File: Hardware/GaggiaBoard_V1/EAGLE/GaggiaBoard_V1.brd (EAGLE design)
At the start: 87 x 122 mm, 113 parts, among them IC1 LD117ADT33TR, J10 PIN262409-1, J11 PIN262409-1, J12 PIN262409-1, J13 PIN262409-1, J14 PIN262409-1, J15 PIN262409-1, J16 PIN262409-1, J17 PIN262409-1, J18 PIN262409-1, J19 PIN262409-1, J2 QWIIC_RIGHT_ANGLE, J20 PIN262409-1, J21 PIN262409-1, J22 PIN262409-1, J23 PIN262409-1, J24 5033981892, J3 QWIIC_RIGHT_ANGLE, J4 1X2-3.5MM, J5 1X2-3.5MM, K1 RELAY-SPDT-JZC-11F, K2 RELAY-SPDT-JZC-11F, K3 RELAY-SPDT-JZC-11F, Q1 600mA/40V, Q2 600mA/40V, Q3 600mA/40V, Q4 600mA/40V, Q5 600mA/40V, Q6 600mA/40V, Q8 600mA/40V, Q9 600mA/40V, U1 BLACKPILL, U2 MAX31855K, U3 MAX31855K, U5 TXS0102, U6 TXU0102

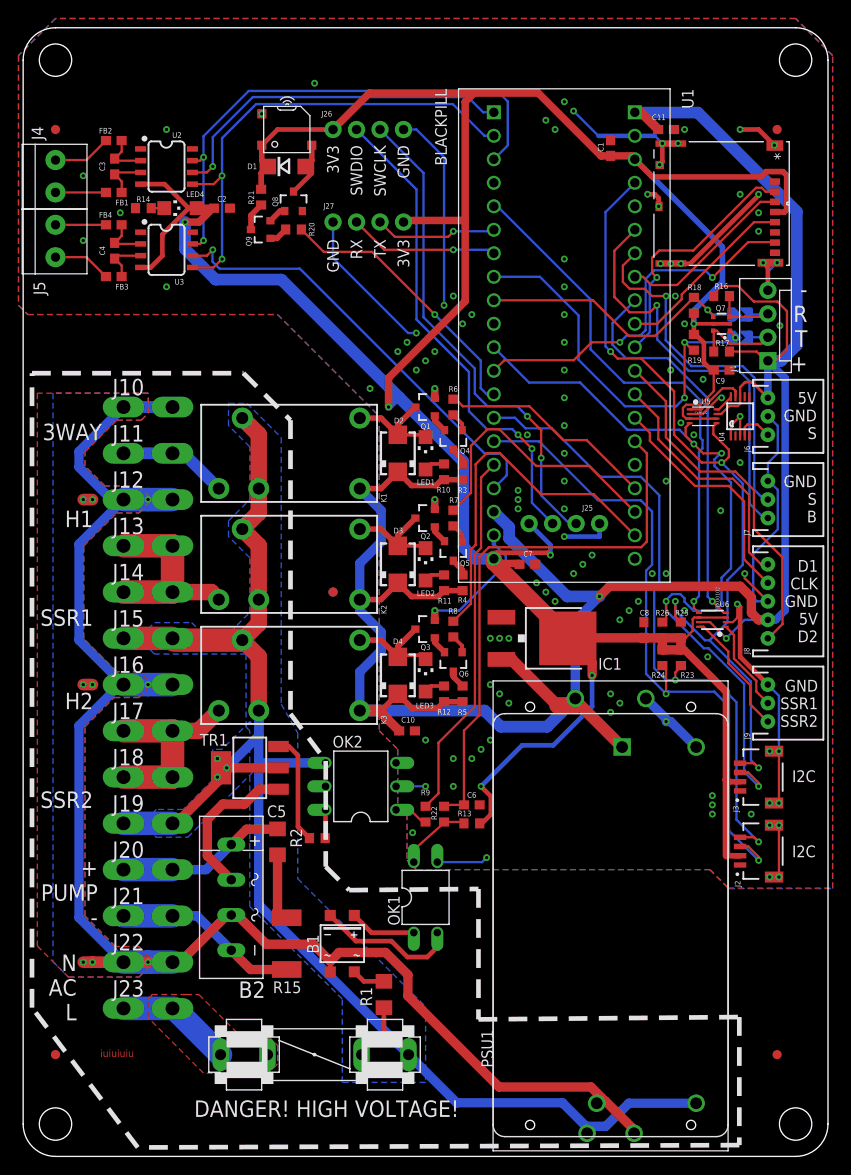
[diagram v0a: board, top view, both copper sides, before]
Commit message: Connectors spacing fixed
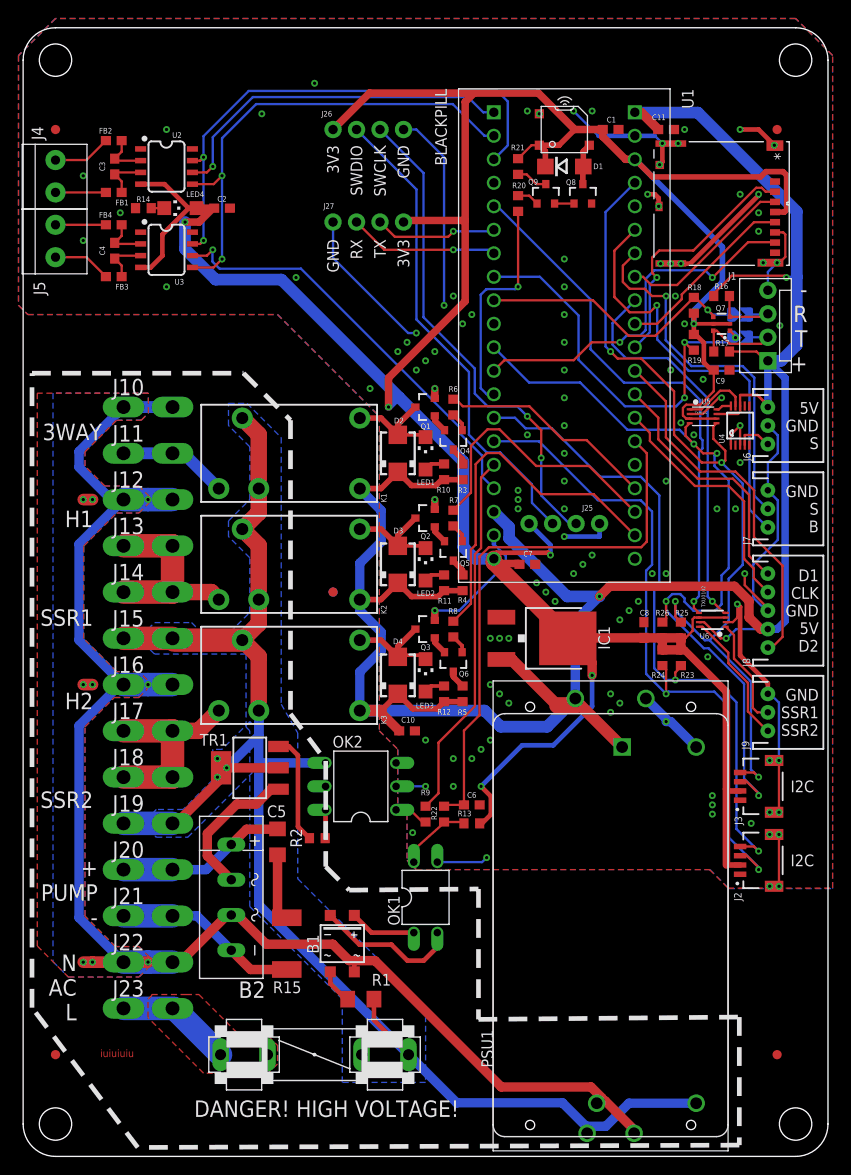
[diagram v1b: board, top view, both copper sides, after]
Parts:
- moved Q8 31.3 mm to (57.0, 93.0)
- moved Q9 31.0 mm to (53.0, 93.0), turned to 0 degrees
- moved D1 30.0 mm to (55.0, 96.0)
- moved SPK1 30.0 mm to (55.0, 100.0)
- moved R21 28.0 mm to (50.0, 96.0)
- moved R20 24.4 mm to (50.0, 92.0), turned to 90 degrees
- moved R1 2.55 mm to (33.0, 6.00), turned to 180 degrees
- moved C1 2.00 mm to (60.0, 100.0), turned to 0 degrees
- moved J2 1.00 mm to (74.0, 21.0)
- moved J3 1.00 mm to (74.0, 29.0)
- moved J6 1.00 mm to (77.0, 68.0)
- moved J7 1.00 mm to (77.0, 59.0)
- moved J8 1.00 mm to (77.0, 48.0)
- moved J9 1.00 mm to (77.0, 37.0)
- moved U4 1.00 mm to (74.0, 68.0)
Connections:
- net AC_N: now also B1.~2; no longer B1.~1
- net N$37: now also B1.~1; no longer B1.~2
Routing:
- net PB5: track 29.9 -> 24.3 mm
- net 5V: track 280.2 -> 275.5 mm, vias 2 -> 3
- net GND: track 183.1 -> 186.1 mm, vias 115 -> 116
- net 3V3: track 349.5 -> 347.3 mm
- net N$30: track 6.75 -> 4.49 mm
- net SPI2_NSS2: track 48.1 -> 46.0 mm
- net AC_N: track 169.8 -> 167.7 mm
- net N$42: track 10.1 -> 11.8 mm
- net AC_P: track 172.6 -> 174.0 mm
- net PA3: track 38.5 -> 39.7 mm
- net I2C1_SCL: track 70.8 -> 71.8 mm
- net PA1: track 26.0 -> 26.9 mm
- net N$41: track 13.7 -> 14.6 mm
- net I2C1_SDA: track 72.7 -> 73.6 mm
- net N$40: track 16.6 -> 15.7 mm
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
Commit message: Layout update
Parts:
- added C12: 1nF/250V, rcl:C0603
- added C13: 10uF/16V, rcl:C0603
- added D5: 1N4007, diode:DO214AC
- added IC2: LD117AS33TR, v-reg:SOT223
- added Q10: 600mA/40V, SparkFun-DiscreteSemi:SOT23-3
- added R27, R28: 10K, rcl:R0603
- IC1: value LD117ADT33TR -> LD117AS33TR; device v-reg:DPACK -> v-reg:SOT223
- J2, J3: value QWIIC_RIGHT_ANGLE -> Vertical Qwiic Connector; device SparkFun-Connectors:JST04_1MM_RA -> SparkFun-Connectors:JST04_1MM_VERT
- J6, J7, J9: device SparkFun-Connectors:JST-3-PTH -> SparkFun-Connectors:JST-3-PTH-VERT
- J8: device SparkFun-Connectors:JST-5-PTH -> SparkFun-Connectors:JST-5-PTH-VERT
- R1: value 220K -> 470; device rcl:R1206 -> rcl:R0603
- R12: value 120 -> 51
- R13: value 10K -> 220; device rcl:R0603 -> rcl:R2512
- R14: value 51 -> 10K
- R15: value 220 -> 1K; device rcl:R2512 -> rcl:R0603
- R20, R21: value 10K -> 220K; device rcl:R0603 -> rcl:R1206
- R22: value 100 -> 22K
- R9: value 470 -> 120
- moved R21 91.2 mm to (30.0, 7.00), turned to 0 degrees
- moved R20 85.8 mm to (38.0, 7.00), turned to 180 degrees
- moved R14 73.6 mm to (43.0, 26.0), turned to 90 degrees
- moved R12 53.3 mm to (20.0, 87.5), turned to 90 degrees
- moved R9 37.1 mm to (42.0, 63.0)
- moved R13 23.9 mm to (25.0, 12.0), turned to 90 degrees
- moved R1 21.2 mm to (40.0, 26.0), turned to 270 degrees
- moved C6 17.6 mm to (39.0, 10.5)
- moved R22 16.6 mm to (30.0, 14.5), turned to 270 degrees
- moved R15 14.0 mm to (39.0, 12.5), turned to 0 degrees
- moved R10 12.0 mm to (42.0, 51.0)
- moved R11 12.0 mm to (42.0, 39.0)
- moved J1 7.65 mm to (78.5, 82.5), turned to 270 degrees
- moved LED4 6.52 mm to (20.0, 92.0), turned to 180 degrees
- moved C2 5.39 mm to (20.0, 96.5), turned to 90 degrees
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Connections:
- new net N$43: C6.2, D5.A, Q10.2
- new net N$44: OK1.1, R15.2
- new net N$45: B1.+, C6.1, R15.1, R22.2
- net 3V3: now also C13.1, IC2.4, R14.2, R27.2; no longer R13.2, R21.2
- net 5V: now also IC2.3, R9.2; no longer R12.2
- net AC_N: now also R21.1; no longer B1.~2
- net AC_P: now also R20.1; no longer R1.1
- net GND: now also C13.2, IC2.1, R12.1; no longer C6.2, R14.1
- net N$2: now also B1.-, D5.C, Q10.1, R22.1; no longer B1.+, OK1.1
- net N$24: now also R9.1; no longer R10.1
- net N$27: now also R12.2; no longer R14.2
- net N$28: now also R10.1; no longer R11.1
- net N$29: now also R11.1; no longer R12.1
- net N$32: now also R13.2; no longer R15.2
- net N$34: now also R28.2; no longer R20.2
- net N$35: now also R27.1; no longer R21.1
- net N$36: now also B1.~1, C12.2, R21.2; no longer OK1.4, R13.1, R22.1
- net N$37: now also B1.~2, C12.1, R20.2; no longer B1.~1, R1.2
- net N$39: now also R1.2; no longer R9.2
- net N$7: now also Q10.3; no longer B1.-
- net PA0: now also OK1.4, R14.1; no longer C6.1, R22.2
- net PB5: now also R28.1; no longer R20.1
- net PB8: now also R1.1; no longer R9.1
- net PUMP_N: now also R13.1; no longer R15.1
- net UART6_5V_RX: now also J1.2; no longer J1.3
- net UART6_5V_TX: now also J1.3; no longer J1.2
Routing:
- net 3V3: track 347.3 -> 274.2 mm, vias 6 -> 3
- net 5V: track 275.5 -> 319.6 mm, vias 3 -> 6
- net N$2: track 7.20 -> 23.5 mm
- net PA0: track 59.9 -> 74.5 mm
- net N$43: track 0.00 -> 12.4 mm
- net I2C2_SDA: track 87.3 -> 75.0 mm, vias 4 -> 3
- net N$7: track 15.8 -> 3.62 mm
- net PA1: track 26.9 -> 38.8 mm
- net N$45: track 0.00 -> 11.8 mm
- net GND: track 186.1 -> 174.6 mm, vias 116 -> 120
- net I2C2_SCL: track 94.1 -> 82.7 mm
- net PA3: track 39.7 -> 29.7 mm
- net AC_N: track 167.7 -> 176.6 mm
- net PA2: track 27.6 -> 34.0 mm
- net N$22: track 1.70 -> 6.31 mm
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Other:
- board text added: "+ R T -"
- board text added: "B S GND"
- board text added: "D2 5V GND CLK D1"
- board text added: "S GND 5V"
- board text removed: "- R T +"
- board text removed: "5V GND S"
- board text removed: "D1 CLK GND 5V D2"
- board text removed: "GND S B"

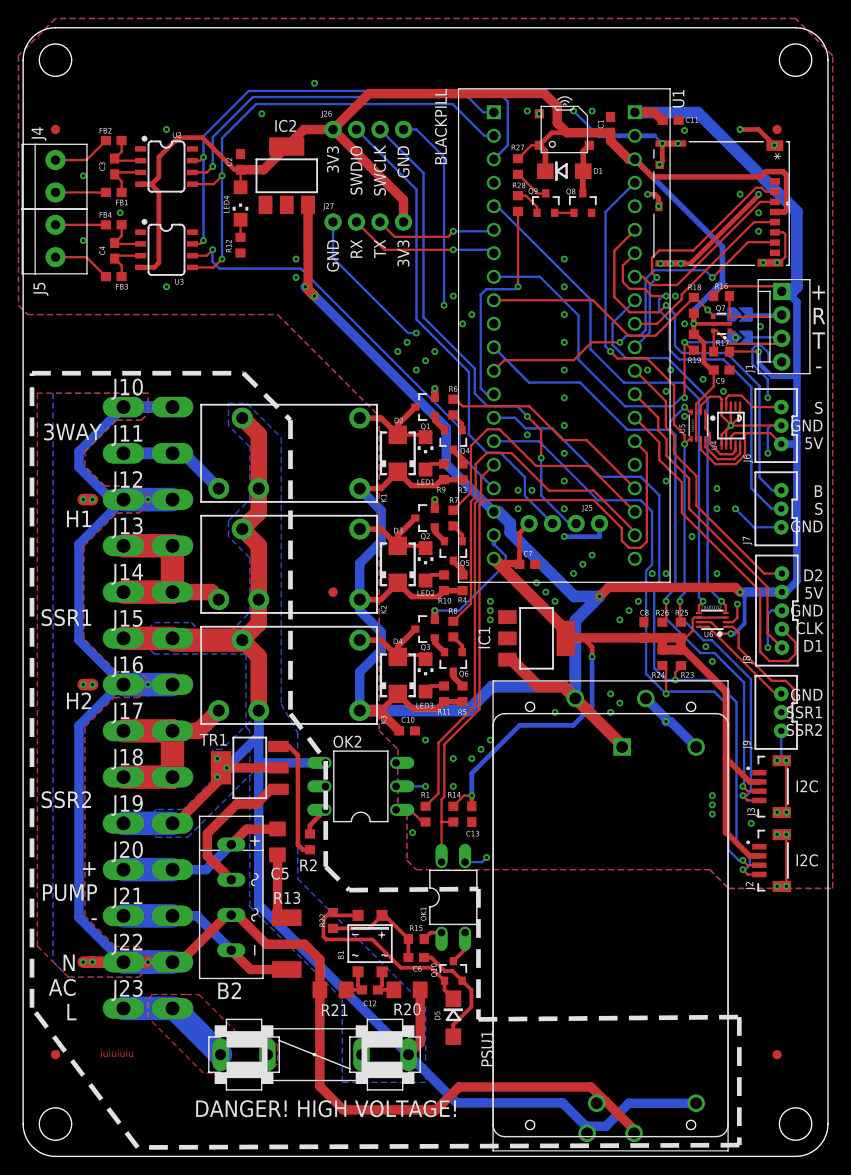
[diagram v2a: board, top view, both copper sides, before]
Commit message: Scales port change to PB
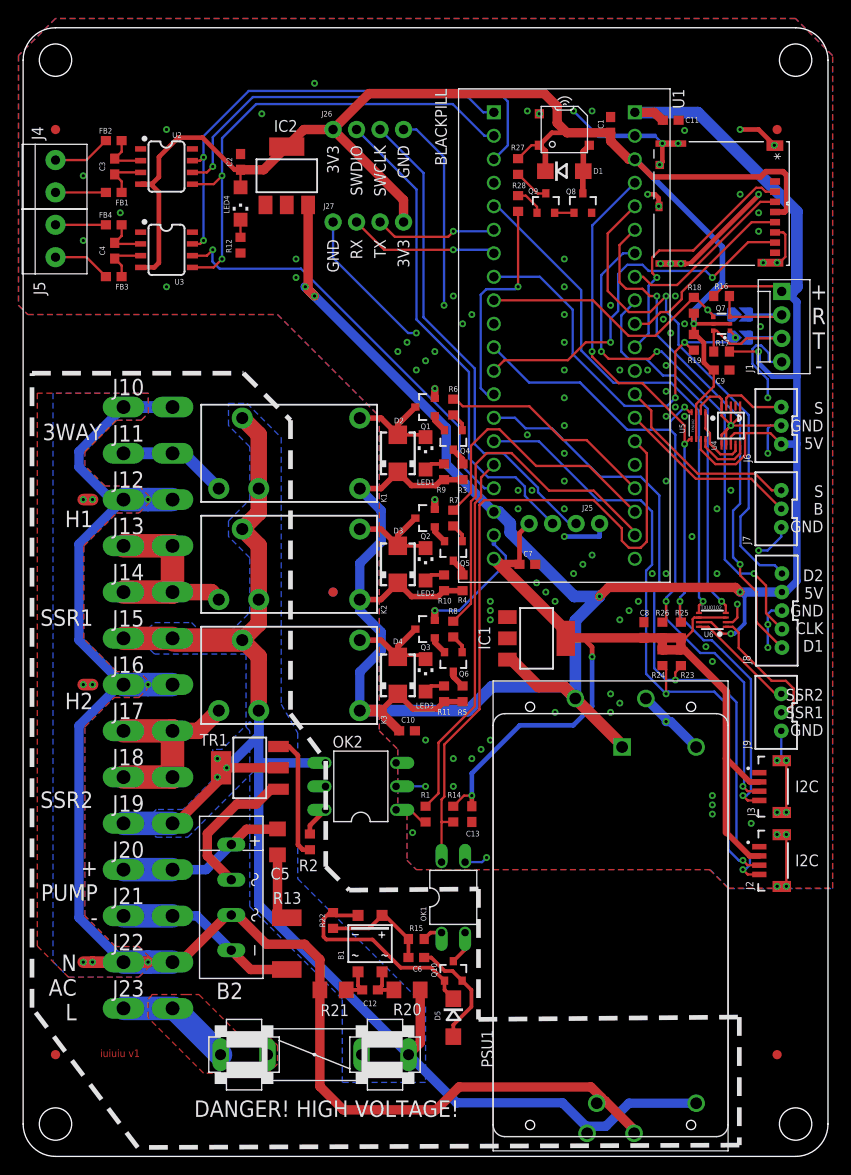
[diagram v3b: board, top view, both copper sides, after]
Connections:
- removed net PA3: J8.5, U1.P2$12
- new net PB2: J8.5, U1.P2$5
- net PA1: now also J7.2; no longer J8.2
- net PA2: now also J7.3; no longer J8.1
- net PB0: now also J8.2; no longer J7.2
- net PB1: now also J8.1; no longer J7.3
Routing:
- net PB2: track 0.00 -> 55.2 mm, vias 0 -> 1
- net PA3: track 29.7 -> 0.00 mm
- net PA1: track 38.8 -> 19.9 mm
- net PB0: track 41.4 -> 56.4 mm, vias 1 -> 3
- net PA2: track 34.0 -> 21.2 mm
- net PB1: track 43.3 -> 55.2 mm, vias 1 -> 2
- net GND: track 174.6 -> 172.9 mm, vias 120 -> 125
- net PA6: track 42.5 -> 40.9 mm
- net SPI1_MISO: track 40.1 -> 41.2 mm
- net SWDIO: track 52.2 -> 53.1 mm
- net I2C2_SCL: track 82.7 -> 83.6 mm
- net SWCLK: track 53.7 -> 53.0 mm, vias 2 -> 0
- net UART6_TX: track 44.2 -> 43.6 mm
- net SPI2_NSS2: track 46.0 -> 46.6 mm
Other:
- board text added: "S B GND"
- board text added: "SSR2 SSR1 GND"
- board text added: "iuiuiu v1"
- board text removed: "B S GND"
- board text removed: "GND SSR1 SSR2"
- board text removed: "iuiuiuiu"

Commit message: Pump bridge rectifier removed, SSR control changed
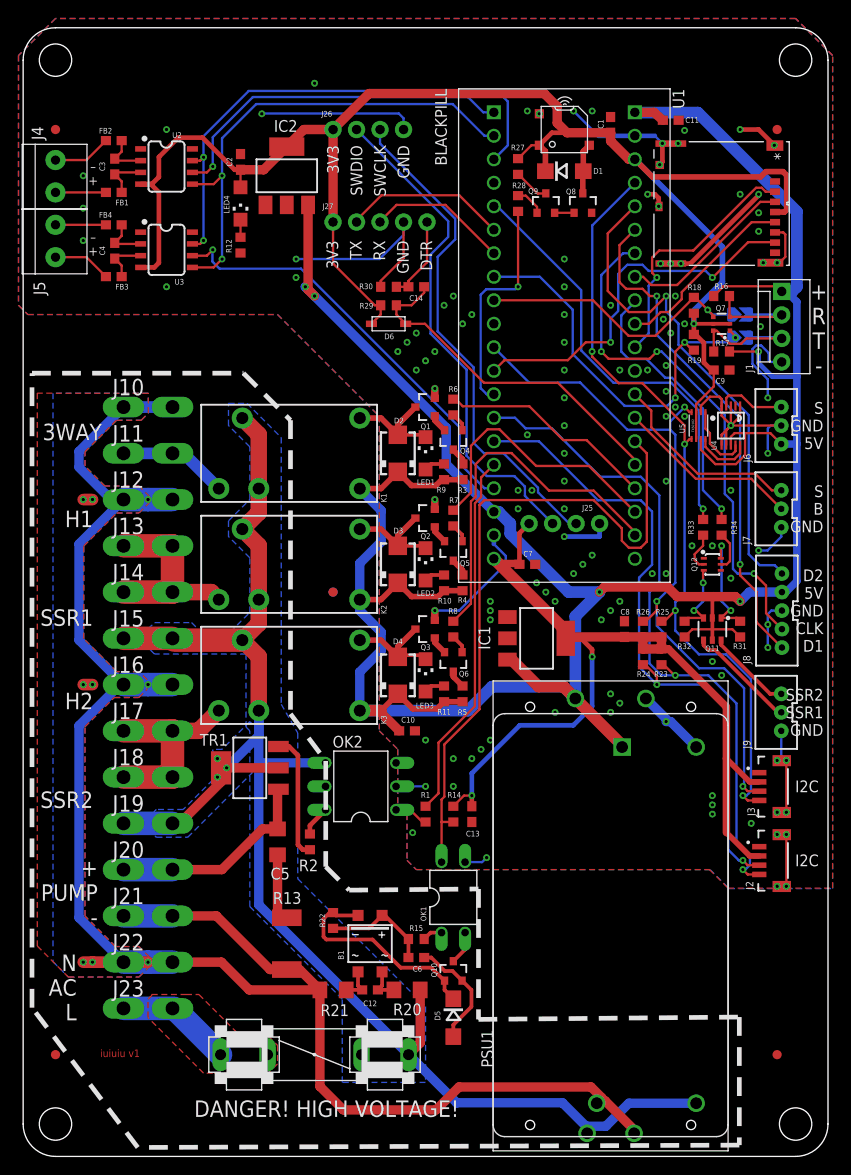
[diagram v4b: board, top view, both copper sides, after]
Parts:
- removed B2: RECTIFIER-2KBP, rectifier:2KBP
- removed U6: TXU0102, microbuilder:VFSOP-8
- added C14: 0.1uF, rcl:C0603
- added D6: (no value), adafruit:SOD-123
- added Q11: (no value), SparkFun-DiscreteSemi:SOT26
- added Q12: (no value), SparkFun-DiscreteSemi:SC70-6
- added R29, R33, R34: 10K, rcl:R0603
- added R30: 1K, rcl:R0603
- added R31, R32: 120K, rcl:R0603
- J27: device SparkFun-Connectors:1X04_NO_SILK -> SparkFun-Connectors:1X05_NO_SILK
- moved J27 7.62 mm to (30.0, 90.0), turned to 0 degrees
- moved C8 2.10 mm to (61.5, 46.0)
- moved R23 2.10 mm to (65.5, 43.0)
- moved R24 2.10 mm to (63.5, 43.0)
- moved R25 2.10 mm to (65.5, 46.0)
- moved R26 2.10 mm to (63.5, 46.0)
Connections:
- removed net N$40: B2.AC2, TR1.1
- removed net PUMP_N: B2.-, J21.A1, J21.A2, R13.1
- new net N$46: Q12.2, R33.1
- new net N$47: Q11.G2, Q12.3, R32.1
- new net N$48: Q11.G1, Q12.6, R31.1
- new net N$49: Q12.5, R34.1
- new net NRST: C14.2, D6.A, R29.1, U1.P2$16
- new net RTS: C14.1, J27.5, R30.2
- net 3V3: now also D6.C, R29.2; no longer U6.3, U6.6
- net 5V: now also Q11.S1, Q11.S2, R31.2, R32.2; no longer U6.7
- net AC_N: now also J21.A1, J21.A2, R13.1; no longer B2.AC1
- net GND: now also Q12.1, Q12.4, R30.1; no longer U6.2
- net N$41: now also J9.2, Q11.D2; no longer J9.3, U6.8
- net N$42: now also J9.3, Q11.D1; no longer J9.2, U6.1
- net PA6: now also R34.2; no longer U6.4
- net PA8: now also R33.2; no longer U6.5
- net PUMP_P: now also TR1.1; no longer B2.+
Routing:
- net NRST: track 0.00 -> 38.0 mm
- net PUMP_N: track 20.1 -> 0.00 mm
- net AC_N: track 176.6 -> 195.0 mm
- net N$40: track 15.7 -> 0.00 mm
- net N$48: track 0.00 -> 12.4 mm, vias 0 -> 2
- net PA6: track 40.9 -> 30.3 mm
- net PA8: track 57.4 -> 47.1 mm
- net RTS: track 0.00 -> 9.13 mm
- net N$47: track 0.00 -> 8.37 mm, vias 0 -> 2
- net N$42: track 14.4 -> 9.20 mm
- net UART1_TX: track 13.3 -> 17.7 mm, vias 1 -> 0
- net PUMP_P: track 18.5 -> 22.8 mm
- net N$49: track 0.00 -> 4.30 mm
- net N$46: track 0.00 -> 4.25 mm
- net 3V3: track 274.2 -> 277.5 mm
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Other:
- board text added: "3V3 TX RX GND DTR"
- board text added: "– + – +"
- board text removed: "GND RX TX 3V3"
